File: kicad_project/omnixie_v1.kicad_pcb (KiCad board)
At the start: 2 copper layers, 19.1 x 31.8 mm, 59 parts, among them J1 Conn_01x04, J2 SM04B-SRSS-TB, J3 SM04B-SRSS-TB, J4 USB4105-GF-A, J5 Conn_01x04, J6 Conn_01x02, J7 Conn_01x02, Q0 BSS123, Q1 BSS123, Q10 BSS123, Q11 BSS123, Q12 IPN50R1K4CEATMA1, Q2 BSS123, Q3 BSS123, Q4 BSS123, Q5 BSS123, Q6 BSS123, Q7 BSS123, Q8 BSS123, Q9 BSS123, T2 ATB322515-0110, U1 CH32V003F4U6, U3 PI4IOE5V6416ZDEX, U4 XC6206P332MR

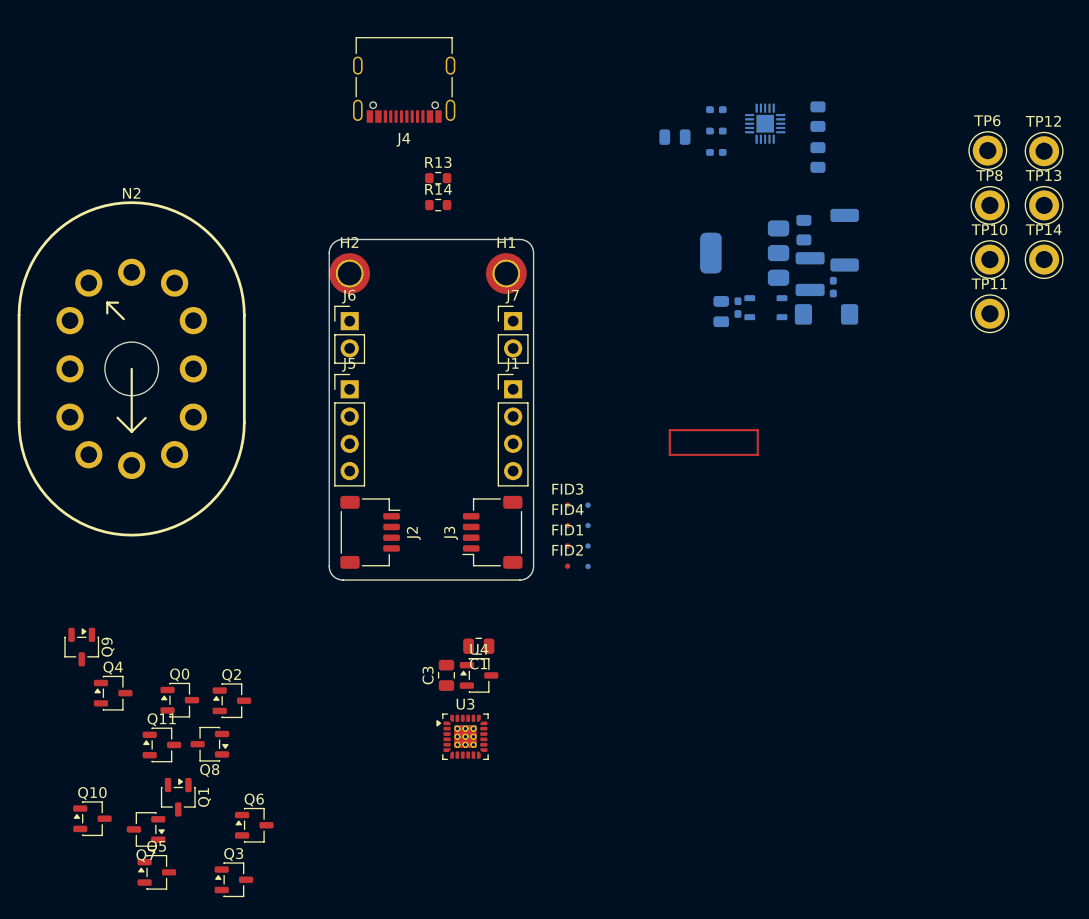
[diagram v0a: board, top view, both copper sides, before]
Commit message: component placement commencing
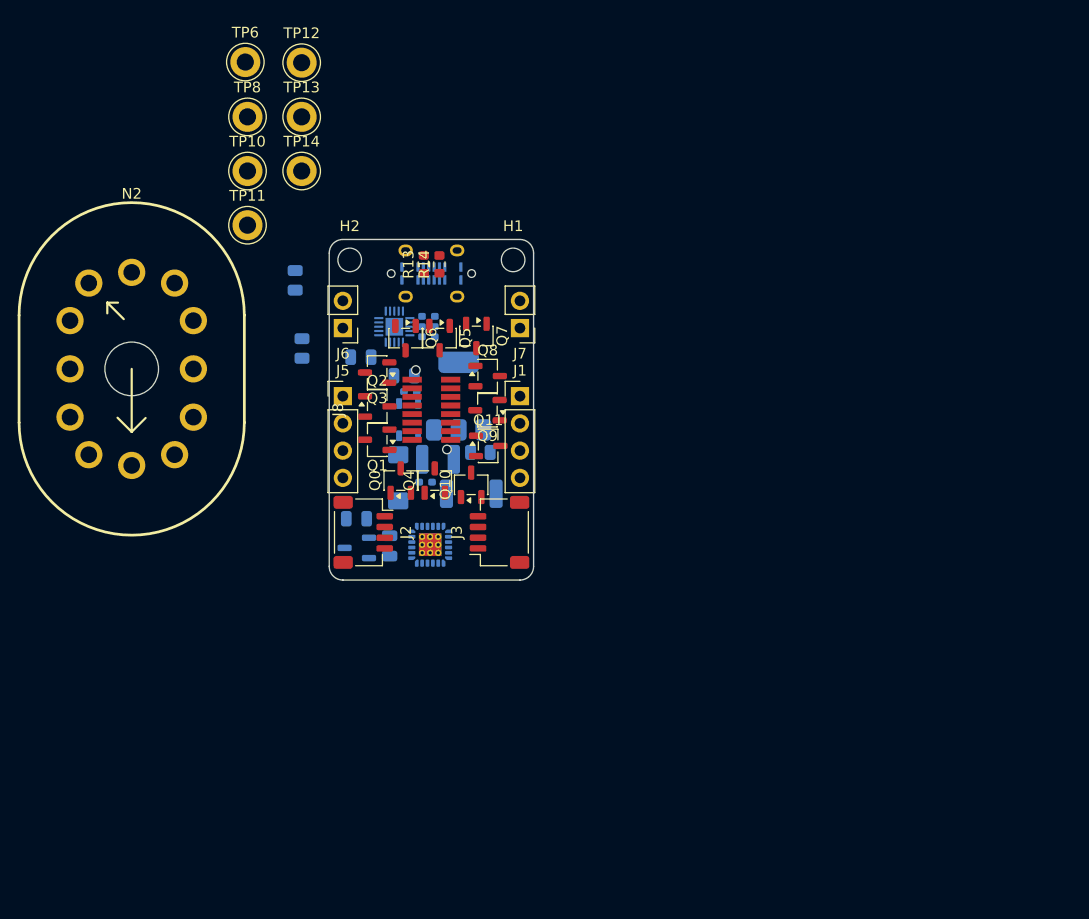
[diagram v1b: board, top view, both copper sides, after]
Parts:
- removed FID1, FID2, FID3, FID4, FID5, FID6, FID7, FID8: Fiducial, Fiducial:Fiducial_0.5mm_Mask1mm
- removed T2: ATB322515-0110, OMNIXIE:ATB322515
- added J8: IL-WX-16S-VF-B-E1000E, OMNIXIE:IL-WX-16S-VF-B-E1000E-SOCKET, F.Cu at (148.3, 96.2)
- added T1: ATB322515-0110, OMNIXIE:ATB322515, B.Cu at (146.2, 97.1)
- C1, C3, U3, U4: moved to B.Cu
- H1, H2: footprint MountingHole:MountingHole_2.2mm_M2_DIN965_Pad_TopOnly -> MountingHole:MountingHole_2.2mm_M2
- J4: footprint Connector_USB:USB_C_Receptacle_Palconn_UTC16-G -> OMNIXIE:USB4120-03-C; moved to B.Cu
- moved TP10 69.7 mm to (131.2, 73.9)
- moved TP11 69.7 mm to (131.2, 78.9)
- moved TP12 69.7 mm to (136.2, 63.8)
- moved TP13 69.7 mm to (136.2, 68.8)
- moved TP14 69.7 mm to (136.2, 73.9)
- moved TP6 69.7 mm to (131.0, 63.7)
- moved TP8 69.7 mm to (131.2, 68.8)
- moved Q5 56.4 mm to (149.1, 89.5), turned to -90 degrees
- moved Q7 55.4 mm to (152.5, 89.3), turned to -90 degrees
- moved R11 51.3 mm to (136.3, 90.4)
- moved R7 51.1 mm to (135.6, 84.1), turned to 90 degrees
- moved Q3 49.1 mm to (143.3, 92.7), turned to 180 degrees
- moved Q6 47.6 mm to (145.9, 89.5), turned to -90 degrees
- moved Q10 47.1 mm to (152.0, 103.2), turned to 90 degrees
- moved Q9 43.8 mm to (153.6, 96.2), turned to 180 degrees
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- renumbered D2 to D1
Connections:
- net Net-(D2-A) renamed /D_1
- net Net-(D2-K) renamed /D_2
- net Net-(J4-CC1) renamed /CC1
- net Net-(J4-CC2) renamed /CC2
- net Net-(R3-Pad1) renamed /<NO NET>
- net Net-(R5-Pad1) renamed /HV_1
- net VIN renamed +5V
- R15 pad 2: Net-(U1-PD4/A7/UCK/T2CH1ETR/OPO/T1CH4ETR) -> D-
- R8 pad 2: Net-(U1-PD4/A7/UCK/T2CH1ETR/OPO/T1CH4ETR) -> D-
- R9 pad 2: Net-(U1-PD3/A4/T2CH2/AETR/UCTS/T1CH4) -> D+
- U1 pad 17: Net-(U1-PD3/A4/T2CH2/AETR/UCTS/T1CH4) -> D+
- U1 pad 18: Net-(U1-PD4/A7/UCK/T2CH1ETR/OPO/T1CH4ETR) -> D-

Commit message: more component placement
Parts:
- moved TP12 17.7 mm to (152.8, 70.1)
- moved TP14 15.8 mm to (152.1, 74.8)
- moved TP10 15.0 mm to (145.2, 68.4)
- moved J7 11.9 mm to (168.5, 88.3)
- moved TP11 11.8 mm to (138.4, 69.6)
- moved J1 11.4 mm to (168.0, 93.8)
- moved C5 10.6 mm to (143.1, 103.3)
- moved R12 9.25 mm to (149.7, 91.4)
- moved R6 8.64 mm to (154.3, 95.6), turned to -90 degrees
- moved R3 8.04 mm to (141.9, 101.2), turned to -90 degrees
- moved R5 6.24 mm to (152.3, 98.5), turned to -90 degrees
- moved TP13 6.15 mm to (140.5, 73.3)
- moved D1 5.01 mm to (150.0, 101.0), turned to 180 degrees
- moved T1 4.23 mm to (144.6, 101.0), turned to 0 degrees
- moved Q12 3.69 mm to (147.4, 96.0), turned to 180 degrees
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
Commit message: reworking the board. Its a prototype not production ready
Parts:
- removed H1, H2: MountingHole, MountingHole:MountingHole_2.2mm_M2
- removed J7: Conn_01x02, Connector_PinHeader_2.54mm:PinHeader_1x02_P2.54mm_Vertical
- removed N2: IN-12BORIGINAL, NIXIE:IN-12A Nixie
- added ?: , clipboard:fd3e1fcc-ecdd-4f52-861b-fe5b40741508, F.Cu at (103.4, 94.6)
- added ?: , clipboard:011728ca-3ec8-4c00-b368-afb68c2a849a, F.Cu at (94.8, 139.5)
- added D2: GREEN, LED_SMD:LED_0603_1608Metric, F.Cu at (131.9, 138.9)
- added D8: GREEN, LED_SMD:LED_0603_1608Metric, F.Cu at (123.0, 146.8)
- added FID10: Fiducial, Fiducial:Fiducial_0.5mm_Mask1mm, F.Cu at (129.5, 157.1)
- added FID11: Fiducial, Fiducial:Fiducial_0.5mm_Mask1mm, F.Cu at (129.5, 159.6)
- added FID12: Fiducial, Fiducial:Fiducial_0.5mm_Mask1mm, F.Cu at (129.5, 162.2)
- added FID13: Fiducial, Fiducial:Fiducial_0.5mm_Mask1mm, F.Cu at (132.0, 154.5)
- added FID14: Fiducial, Fiducial:Fiducial_0.5mm_Mask1mm, F.Cu at (132.0, 157.1)
- added FID15: Fiducial, Fiducial:Fiducial_0.5mm_Mask1mm, F.Cu at (132.0, 159.6)
- added FID9: Fiducial, Fiducial:Fiducial_0.5mm_Mask1mm, F.Cu at (129.5, 154.5)
- added JP4: SMT_THERM_JMP, Jumper:SolderJumper-2_P1.3mm_Bridged_RoundedPad1.0x1.5mm, F.Cu at (123.2, 140.2)
- added JP5: TH_THERM_JMP, Jumper:SolderJumper-2_P1.3mm_Open_RoundedPad1.0x1.5mm, F.Cu at (123.2, 143.8)
- added R10: 10k, Resistor_SMD:R_0402_1005Metric, F.Cu at (126.5, 146.5)
- added R16: 10k, Resistor_SMD:R_0402_1005Metric, F.Cu at (131.3, 141.2)
- C3, C4, C5: footprint Capacitor_SMD:C_0805_2012Metric -> Capacitor_SMD:C_0603_1608Metric
- J1: value Conn_01x04 -> Conn_01x10; footprint Connector_PinHeader_2.54mm:PinHeader_1x04_P2.54mm_Vertical -> Connector_PinHeader_2.54mm:PinHeader_1x10_P2.54mm_Vertical
- J6: footprint Connector_PinHeader_2.54mm:PinHeader_1x02_P2.54mm_Vertical -> Connector_PinHeader_2.54mm:PinHeader_1x03_P2.54mm_Vertical
- R11, R12: footprint Resistor_SMD:R_0805_2012Metric -> Resistor_SMD:R_0603_1608Metric
- R3, R5: value 4.42m -> 10m; footprint Resistor_SMD:R_0402_1005Metric_Pad0.72x0.64mm_HandSolder -> Resistor_SMD:R_0603_1608Metric
- R7: footprint Resistor_SMD:R_0805_2012Metric -> Resistor_SMD:R_0402_1005Metric_Pad0.72x0.64mm_HandSolder
- moved R13 86.9 mm to (209.8, 142.6), turned to -90 degrees
- moved R14 84.5 mm to (208.3, 142.7), turned to -90 degrees
- moved J4 82.0 mm to (209.8, 137.7), turned to 180 degrees
- moved J2 81.3 mm to (201.7, 52.4), turned to 90 degrees
- moved R9 76.7 mm to (210.1, 132.3), turned to 90 degrees
- moved TP13 75.5 mm to (141.5, 148.9)
- moved R8 75.4 mm to (209.2, 132.3), turned to 90 degrees
- moved C4 73.5 mm to (201.9, 133.1), turned to 0 degrees
- moved U1 72.2 mm to (203.6, 130.2)
- moved R15 72.2 mm to (206.9, 130.9)
- moved C1 64.3 mm to (199.4, 134.0), turned to -90 degrees
- moved U4 60.7 mm to (196.6, 134.0), turned to 90 degrees
- moved C3 59.3 mm to (196.7, 136.8), turned to 0 degrees
- moved J3 59.1 mm to (176.5, 52.7), turned to -90 degrees
- moved TP8 57.8 mm to (153.4, 122.2)
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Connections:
- C5 pad 1: +5V -> +5V_FLY
- J1 pad 1: I2C_SDA -> PD2
- J1 pad 2: I2C_SCL -> PC6
- J1 pad 3: +3V3 -> PC5
- J1 pad 4: GND -> PC1
- J5 pad 1: I2C_SDA -> I2C_SCL
- J5 pad 2: I2C_SCL -> I2C_SDA
- R15 pad 2: D- -> /D-_1
- R3 pad 2: +5V -> +5V_FLY
- R8 pad 2: D- -> /D-_1
- R9 pad 2: D+ -> /D+_1
- T1 pad 2: +5V -> +5V_FLY
- TP10 pad 1: +5V -> +5V_FLY
- U1 pad 1: unconnected-(U1-PD7/NRST/T2CH4/OPP1/UCK-Pad1) -> PD7
- U1 pad 12: unconnected-(U1-PC5/SCK/T1ETR/T2CH1ETR/SCL/UCK/T1CH3-Pad12) -> PC5
- U1 pad 13: unconnected-(U1-PC6/MOSI/T1CH1CH3/UCTS/SDA-Pad13) -> PC6
- U1 pad 14: unconnected-(U1-PC7/MISO/T1CH2/T2CH2/URTS-Pad14) -> HV_SW
- U1 pad 16: unconnected-(U1-PD2/A3/T1CH1/T2CH3/T1CH2N-Pad16) -> PD2
- U1 pad 17: D+ -> /D+_1
- U1 pad 18: D- -> /D-_1
- U1 pad 2: HV_SW -> PA1
- U1 pad 20: unconnected-(U1-PD6/A7/URX/T2CH3/UTX-Pad20) -> PD6
- U1 pad 3: unconnected-(U1-PA2/OSCO/A0/T1CH2N/OPP0/AETR2-Pad3) -> PA2
- U1 pad 5: unconnected-(U1-PD0/T1CH1N/OPN1/SDA/UTX-Pad5) -> PD0
- U1 pad 7: unconnected-(U1-PC0/T2CH3/UTX/NSS/T1CH3-Pad7) -> PC0
- U1 pad 8: unconnected-(U1-PC1/SDA/NSS/T2CH4/T2CH1ETR/T1BKIN/URX-Pad8) -> PC1
- U3 pad 1: DIG_0 -> DIG_1
- U3 pad 10: DIG_8 -> DIG_9
- U3 pad 11: DIG_9 -> DIG_8
- U3 pad 12: DIG_DP -> DIG_AUX
- U3 pad 13: DIG_AUX -> DIG_DP
- U3 pad 2: DIG_1 -> DIG_0
- U3 pad 21: +3V3 -> Net-(JP4-B)
- U3 pad 23: +3V3 -> Net-(JP4-B)
- U3 pad 3: DIG_2 -> DIG_3
- U3 pad 4: DIG_3 -> DIG_2
- U3 pad 5: DIG_4 -> DIG_5
- U3 pad 6: DIG_5 -> DIG_4
- U3 pad 7: DIG_6 -> DIG_7
- U3 pad 8: DIG_7 -> DIG_6
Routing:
- net DIG_9: track 0.00 -> 14.1 mm, vias 0 -> 1
- net CATH7: track 0.00 -> 11.8 mm, vias 0 -> 2
- net CATH9: track 0.00 -> 11.0 mm, vias 0 -> 2
- net DIG_8: track 0.00 -> 10.7 mm, vias 0 -> 1
- net DIG_7: track 0.00 -> 10.3 mm, vias 0 -> 1
- net GND: track 0.00 -> 10.3 mm, vias 0 -> 6
- net CATH5: track 0.00 -> 9.98 mm, vias 0 -> 2
- net DIG_6: track 0.00 -> 9.98 mm, vias 0 -> 1
- net D-: track 0.00 -> 9.70 mm, vias 0 -> 2
- net DIG_AUX: track 0.00 -> 9.50 mm, vias 0 -> 1
- net DIG_1: track 0.00 -> 8.88 mm, vias 0 -> 1
- net CATHAUX: track 0.00 -> 8.72 mm, vias 0 -> 2
- net CATH3: track 0.00 -> 8.40 mm, vias 0 -> 2
- net CATH1: track 0.00 -> 8.32 mm, vias 0 -> 2
- net DIG_5: track 0.00 -> 8.16 mm, vias 0 -> 1
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- added copper zone on B.Cu, net GND
- added copper zone on F.Cu, net GND
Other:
- board size 19.1 x 31.8 mm -> 35.6 x 33 mm

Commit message: new component placement pretty much done
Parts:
- removed J2, J3: SM04B-SRSS-TB, Connector_JST:JST_SH_SM04B-SRSS-TB_1x04-1MP_P1.00mm_Horizontal
- C2, C5, D1, Q12, R12, R3, R5, R6, R7, T1: moved to F.Cu
- JP5, TP10, TP11, TP12, TP14, TP6, TP8: moved to B.Cu
- moved FID10 110.6 mm to (145.6, 47.7)
- moved FID12 110.6 mm to (145.6, 52.8)
- moved FID13 110.6 mm to (148.1, 45.1)
- moved FID14 110.6 mm to (148.1, 47.7)
- moved FID9 110.6 mm to (145.6, 45.1)
- moved FID11 110.6 mm to (145.6, 50.2)
- moved FID15 110.6 mm to (148.1, 50.2)
- moved ? 96.6 mm to (183.6, 101.3)
- moved JP4 80.2 mm to (147.8, 63.9)
- moved R13 76.4 mm to (165.2, 80.6), turned to 0 degrees
- moved R14 73.9 mm to (165.2, 82.6), turned to 0 degrees
- moved J4 71.5 mm to (165.4, 81.7), turned to -90 degrees
- moved R9 70.7 mm to (159.8, 82.6), turned to 180 degrees
- moved R8 69.5 mm to (159.8, 83.5), turned to 180 degrees
- moved C1 66.8 mm to (151.9, 87.1)
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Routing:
- net DIG_9: track 14.1 -> 1.33 mm
- net DIG_8: track 10.7 -> 1.31 mm
- net DIG_AUX: track 9.50 -> 1.33 mm
- net CATH8: track 6.47 -> 0.00 mm
- net CATH9: track 11.0 -> 5.06 mm
- net DIG_DP: track 6.27 -> 1.31 mm
- net CATHDP: track 4.81 -> 0.00 mm
- net CATHAUX: track 8.72 -> 4.96 mm

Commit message: home from christmas in vegas
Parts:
- R11, TP10, TP11, TP12, TP14, TP6, TP8: moved to F.Cu
- moved J5 24.8 mm to (141.2, 64.1), turned to 90 degrees
- moved ? 23.7 mm to (205.5, 92.2)
- moved R11 23.2 mm to (175.5, 85.2), turned to 90 degrees
- moved TP10 20.7 mm to (153.5, 80.9)
- moved TP8 18.2 mm to (138.9, 86.6)
- moved TP14 17.1 mm to (141.8, 68.0)
- moved TP12 16.9 mm to (137.1, 66.2)
- moved TP6 16.0 mm to (151.2, 74.9)
- moved R6 15.9 mm to (137.0, 72.7), turned to -90 degrees
- moved TP13 15.9 mm to (135.2, 79.6), turned to 180 degrees
- moved R3 15.2 mm to (150.5, 79.7), turned to -90 degrees
- moved TP11 14.9 mm to (144.8, 83.5)
- moved JP5 14.7 mm to (149.5, 84.1)
- moved JP4 14.6 mm to (154.4, 77.0), turned to 90 degrees
- moved U4 14.5 mm to (160.8, 78.5), turned to 0 degrees
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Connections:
- U3 pad 10: DIG_9 -> DIG_8
- U3 pad 11: DIG_8 -> DIG_9
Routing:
- net GND: track 10.3 -> 27.7 mm, vias 6 -> 14
- net PC1: track 0.00 -> 12.6 mm
- net PC0: track 0.00 -> 9.87 mm
- net PD0: track 0.00 -> 7.94 mm
- net DIG_9: track 1.33 -> 9.03 mm
- net DIG_AUX: track 1.33 -> 8.56 mm
- net D+: track 6.75 -> 0.00 mm, vias 2 -> 0
- net CATHAUX: track 4.96 -> 11.7 mm
- net PA2: track 0.00 -> 6.59 mm
- net CATH9: track 5.06 -> 10.8 mm
- net DIG_DP: track 1.31 -> 7.00 mm
- net CATHDP: track 0.00 -> 5.33 mm
- net DIG_8: track 1.31 -> 6.59 mm
- net PD6: track 0.00 -> 5.23 mm
- net CATH8: track 0.00 -> 4.84 mm
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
